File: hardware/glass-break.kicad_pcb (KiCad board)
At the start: 2 copper layers, 90 x 57 mm, 25 parts, among them P1 USB_OTG, U11 SPX3819

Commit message: layout update
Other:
- board outline removed
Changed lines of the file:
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@@
     (links 47)
     (no_connects 30)
-    (area 0 0 0 0)
+    (area 113.924999 32.924999 204.075001 129.878601)
     (thickness 1.6)
-    (drawings 6)
+    (drawings 19)
     (tracks 0)
     (zones 0)
@@
     )
   )
-  (gr_line (start 133 87) (end 133 54.5) (angle 90) (layer Edge.Cuts) (width 0.15))
-  (gr_circle (center 133 80) (end 140 80) (layer Edge.Cuts) (width 0.15))
-  (gr_line (start 114 33) (end 114 90) (angle 90) (layer Edge.Cuts) (width 0.15))
-  (gr_line (start 204 33) (end 114 33) (angle 90) (layer Edge.Cuts) (width 0.15))
-  (gr_line (start 204 90) (end 204 33) (angle 90) (layer Edge.Cuts) (width 0.15))
-  (gr_line (start 114 90) (end 204 90) (angle 90) (layer Edge.Cuts) (width 0.15))
+  (gr_line (start 172.5 85.5) (end 172.5 97.5) (angle 90) (layer Margin) (width 0.2))
+  (gr_line (start 205 85.5) (end 172.5 85.5) (angle 90) (layer Margin) (width 0.2))
+  (gr_line (start 172.5 85.5) (end 205 85.5) (angle 90) (layer Margin) (width 0.2))
+  (gr_circle (center 149.5 89) (end 149.5 85.5) (layer Margin) (width 0.2))
+  (gr_line (start 153 85.5) (end 117.5 85.5) (angle 90) (layer Margin) (width 0.2))
+  (gr_line (start 153 98.5) (end 153 85.5) (angle 90) (layer Margin) (width 0.2))
+  (gr_line (start 153 85.5) (end 153 98.5) (angle 90) (layer Margin) (width 0.2))
+  (gr_line (start 193 82.5) (end 193 94.5) (angle 90) (layer Margin) (width 0.2))
+  (gr_line (start 193 82.5) (end 205 82.5) (angle 90) (layer Margin) (width 0.2))
+  (gr_line (start 193 56.5) (end 193 44.5) (angle 90) (layer Margin) (width 0.2))
+  (gr_line (start 205 56.5) (end 193 56.5) (angle 90) (layer Margin) (width 0.2))
+  (gr_line (start 132.5 56.5) (end 132.5 44.5) (angle 90) (layer Margin) (width 0.2))
+  (gr_line (start 120.5 56.5) (end 132.5 56.5) (angle 90) (layer Margin) (width 0.2))
+  (gr_line (start 132.5 82.5) (end 120.5 82.5) (angle 90) (layer Margin) (width 0.2))
+  (gr_line (start 132.5 94.5) (end 132.5 82.5) (angle 90) (layer Margin) (width 0.2))
+  (gr_line (start 120.5 44.5) (end 120.5 94.5) (angle 90) (layer Margin) (width 0.2))
+  (gr_line (start 205 44.5) (end 120.5 44.5) (angle 90) (layer Margin) (width 0.2))
+  (gr_line (start 205 94.5) (end 205 44.5) (angle 90) (layer Margin) (width 0.2))
+  (gr_line (start 120.5 94.5) (end 205 94.5) (angle 90) (layer Margin) (width 0.2))
 )

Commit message: layout update
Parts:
- moved C1 94.1 mm to (238.5, 77.5)
- moved C2 94.1 mm to (238.5, 77.5)
- moved C3 94.1 mm to (238.5, 77.5)
- moved C4 94.1 mm to (238.5, 77.5)
- moved D1 94.1 mm to (238.5, 77.5)
- moved D2 94.1 mm to (238.5, 77.5)
- moved D3 94.1 mm to (238.5, 77.5)
- moved D4 94.1 mm to (238.5, 77.5)
- moved JP1 94.1 mm to (238.5, 77.5)
- moved JP4 94.1 mm to (238.5, 77.5)
- moved JP5 94.1 mm to (238.5, 77.5)
- moved P1 94.1 mm to (238.5, 77.5)
- moved R1 94.1 mm to (238.5, 77.5)
- moved R10 94.1 mm to (238.5, 77.5)
- moved R11 94.1 mm to (238.5, 77.5)
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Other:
- board outline added: 83.5 x 48.5 mm
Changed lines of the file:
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@@
     (area 113.924999 32.924999 204.075001 129.878601)
     (thickness 1.6)
-    (drawings 19)
+    (drawings 31)
     (tracks 0)
     (zones 0)
@@
   )
   (module Capacitors_SMD:C_0805 (layer F.Cu)
-    (at 148.5011 105.0036)
+    (at 238.5011 77.5036)
     (descr "Capacitor SMD 0805, reflow soldering, AVX (see smccp.pdf)")
     (tags "capacitor 0805")
@@
   )
   (module Capacitors_SMD:C_0805 (layer F.Cu)
-    (at 148.5011 105.0036)
+    (at 238.5011 77.5036)
     (descr "Capacitor SMD 0805, reflow soldering, AVX (see smccp.pdf)")
     (tags "capacitor 0805")
@@
   )
   (module Capacitors_SMD:C_0805 (layer F.Cu)
-    (at 148.5011 105.0036)
+    (at 238.5011 77.5036)
     (descr "Capacitor SMD 0805, reflow soldering, AVX (see smccp.pdf)")
     (tags "capacitor 0805")
@@
   )
   (module Capacitors_SMD:C_0805 (layer F.Cu)
-    (at 148.5011 105.0036)
+    (at 238.5011 77.5036)
     (descr "Capacitor SMD 0805, reflow soldering, AVX (see smccp.pdf)")
     (tags "capacitor 0805")
@@
   )
   (module LEDs:LED_0805 (layer F.Cu)
-    (at 148.5011 105.0036)
+    (at 238.5011 77.5036)
     (descr "LED 0805 smd package")
     (tags "LED 0805 SMD")
@@
   )
   (module LEDs:LED_0805 (layer F.Cu)
-    (at 148.5011 105.0036)
+    (at 238.5011 77.5036)
     (descr "LED 0805 smd package")
     (tags "LED 0805 SMD")
@@
   )
   (module LEDs:LED_0805 (layer F.Cu)
-    (at 148.5011 105.0036)
+    (at 238.5011 77.5036)
     (descr "LED 0805 smd package")
     (tags "LED 0805 SMD")
@@
   )
   (module LEDs:LED_0805 (layer F.Cu)
-    (at 148.5011 105.0036)
+    (at 238.5011 77.5036)
     (descr "LED 0805 smd package")
     (tags "LED 0805 SMD")
@@
   )
   (module Pin_Headers:Pin_Header_Angled_1x06 (layer F.Cu)
-    (at 148.5011 105.0036)
+    (at 238.5011 77.5036)
     (descr "Through hole pin header")
     (tags "pin header")
@@
   )
   (module Pin_Headers:Pin_Header_Angled_1x10 (layer F.Cu)
-    (at 148.5011 105.0036)
+    (at 238.5011 77.5036)
     (descr "Through hole pin header")
     (tags "pin header")
@@
   )
   (module Pin_Headers:Pin_Header_Angled_1x10 (layer F.Cu)
-    (at 148.5011 105.0036)
+    (at 238.5011 77.5036)
     (descr "Through hole pin header")
     (tags "pin header")
@@
   )
   (module Connect:USB_Micro-B (layer F.Cu)
-    (at 148.5011 105.0036)
+    (at 238.5011 77.5036)
     (descr "Micro USB Type B Receptacle")
     (tags "USB USB_B USB_micro USB_OTG")
@@
   )
   (module Resistors_SMD:R_0805 (layer F.Cu)
-    (at 148.5011 105.0036)
+    (at 238.5011 77.5036)
     (descr "Resistor SMD 0805, reflow soldering, Vishay (see dcrcw.pdf)")
     (tags "resistor 0805")
@@
   )
   (module Resistors_SMD:R_0805 (layer F.Cu)
-    (at 148.5011 105.0036)
+    (at 238.5011 77.5036)
     (descr "Resistor SMD 0805, reflow soldering, Vishay (see dcrcw.pdf)")
     (tags "resistor 0805")
@@
   )
   (module Resistors_SMD:R_0805 (layer F.Cu)
-    (at 148.5011 105.0036)
+    (at 238.5011 77.5036)
     (descr "Resistor SMD 0805, reflow soldering, Vishay (see dcrcw.pdf)")
     (tags "resistor 0805")
@@
   )
   (module Resistors_SMD:R_0805 (layer F.Cu)
-    (at 148.5011 105.0036)
+    (at 238.5011 77.5036)
     (descr "Resistor SMD 0805, reflow soldering, Vishay (see dcrcw.pdf)")
     (tags "resistor 0805")
@@
   )
   (module Resistors_SMD:R_0805 (layer F.Cu)
-    (at 148.5011 105.0036)
+    (at 238.5011 77.5036)
     (descr "Resistor SMD 0805, reflow soldering, Vishay (see dcrcw.pdf)")
     (tags "resistor 0805")
@@
   )
   (module Resistors_SMD:R_0805 (layer F.Cu)
-    (at 148.5011 105.0036)
+    (at 238.5011 77.5036)
     (descr "Resistor SMD 0805, reflow soldering, Vishay (see dcrcw.pdf)")
     (tags "resistor 0805")
@@
   )
   (module Resistors_SMD:R_0805 (layer F.Cu)
-    (at 148.5011 105.0036)
+    (at 238.5011 77.5036)
     (descr "Resistor SMD 0805, reflow soldering, Vishay (see dcrcw.pdf)")
     (tags "resistor 0805")
@@
   )
   (module Resistors_SMD:R_0805 (layer F.Cu)
-    (at 148.5011 105.0036)
+    (at 238.5011 77.5036)
     (descr "Resistor SMD 0805, reflow soldering, Vishay (see dcrcw.pdf)")
     (tags "resistor 0805")
@@
   )
   (module Resistors_SMD:R_0805 (layer F.Cu)
-    (at 148.5011 105.0036)
+    (at 238.5011 77.5036)
     (descr "Resistor SMD 0805, reflow soldering, Vishay (see dcrcw.pdf)")
     (tags "resistor 0805")
@@
   )
   (module Resistors_SMD:R_0805 (layer F.Cu)
-    (at 148.5011 105.0036)
+    (at 238.5011 77.5036)
     (descr "Resistor SMD 0805, reflow soldering, Vishay (see dcrcw.pdf)")
     (tags "resistor 0805")
@@
   )
   (module Resistors_SMD:R_0805 (layer F.Cu)
-    (at 148.5011 105.0036)
+    (at 238.5011 77.5036)
     (descr "Resistor SMD 0805, reflow soldering, Vishay (see dcrcw.pdf)")
     (tags "resistor 0805")
@@
   )
   (module Resistors_SMD:R_0805 (layer F.Cu)
-    (at 148.5011 105.0036)
+    (at 238.5011 77.5036)
     (descr "Resistor SMD 0805, reflow soldering, Vishay (see dcrcw.pdf)")
     (tags "resistor 0805")
@@
   )
   (module TO_SOT_Packages_SMD:SC-70-5 (layer F.Cu)
-    (at 148.5011 105.0036)
+    (at 238.5011 77.5036)
     (descr "SC70-5 SOT323-5")
     (attr smd)
@@
     )
   )
-  (gr_line (start 172.5 85.5) (end 172.5 97.5) (angle 90) (layer Margin) (width 0.2))
-  (gr_line (start 205 85.5) (end 172.5 85.5) (angle 90) (layer Margin) (width 0.2))
-  (gr_line (start 172.5 85.5) (end 205 85.5) (angle 90) (layer Margin) (width 0.2))
+  (gr_line (start 190 59) (end 191.5 59) (angle 90) (layer Edge.Cuts) (width 0.15))
+  (gr_line (start 190 45) (end 190 59) (angle 90) (layer Edge.Cuts) (width 0.15))
+  (gr_line (start 135 45) (end 190 45) (angle 90) (layer Edge.Cuts) (width 0.15))
+  (gr_line (start 121 80) (end 135 80) (angle 90) (layer Edge.Cuts) (width 0.15))
+  (gr_line (start 121 59) (end 121 80) (angle 90) (layer Edge.Cuts) (width 0.15))
+  (gr_line (start 135 59) (end 121 59) (angle 90) (layer Edge.Cuts) (width 0.15))
+  (gr_line (start 135 45) (end 135 59) (angle 90) (layer Edge.Cuts) (width 0.15))
+  (gr_line (start 204.5 59) (end 191.5 59) (angle 90) (layer Edge.Cuts) (width 0.15))
+  (gr_line (start 204.5 80) (end 204.5 59) (angle 90) (layer Edge.Cuts) (width 0.15))
+  (gr_line (start 190.5 80) (end 204.5 80) (angle 90) (layer Edge.Cuts) (width 0.15))
+  (gr_line (start 190.5 93.5) (end 190.5 80) (angle 90) (layer Edge.Cuts) (width 0.15))
+  (gr_line (start 135 93.5) (end 190.5 93.5) (angle 90) (layer Edge.Cuts) (width 0.15))
+  (gr_line (start 135 80) (end 135 93.5) (angle 90) (layer Edge.Cuts) (width 0.15))
+  (dimension 50 (width 0.3) (layer Margin)
+    (gr_text "50.000 mm" (at 214.35 69.5 270) (layer Margin)
+      (effects (font (size 1.5 1.5) (thickness 0.3)))
+    )
+    (feature1 (pts (xy 206.5 94.5) (xy 215.7 94.5)))
+    (feature2 (pts (xy 206.5 44.5) (xy 215.7 44.5)))
+    (crossbar (pts (xy 213 44.5) (xy 213 94.5)))
+    (arrow1a (pts (xy 213 94.5) (xy 212.413579 93.373496)))
+    (arrow1b (pts (xy 213 94.5) (xy 213.586421 93.373496)))
+    (arrow2a (pts (xy 213 44.5) (xy 212.413579 45.626504)))
+    (arrow2b (pts (xy 213 44.5) (xy 213.586421 45.626504)))
+  )
+  (dimension 84.5 (width 0.3) (layer Margin)
+    (gr_text "84.500 mm" (at 162.75 100.85) (layer Margin)
+      (effects (font (size 1.5 1.5) (thickness 0.3)))
+    )
+    (feature1 (pts (xy 205 96) (xy 205 102.2)))
+    (feature2 (pts (xy 120.5 96) (xy 120.5 102.2)))
+    (crossbar (pts (xy 120.5 99.5) (xy 205 99.5)))
+    (arrow1a (pts (xy 205 99.5) (xy 203.873496 100.086421)))
+    (arrow1b (pts (xy 205 99.5) (xy 203.873496 98.913579)))
+    (arrow2a (pts (xy 120.5 99.5) (xy 121.626504 100.086421)))
+    (arrow2b (pts (xy 120.5 99.5) (xy 121.626504 98.913579)))
+  )
+  (gr_circle (center 176 89) (end 172.5 89.5) (layer Margin) (width 0.2))
+  (gr_circle (center 176 50) (end 172.5 50) (layer Margin) (width 0.2))
+  (gr_circle (center 149.5 50) (end 153 49.5) (layer Margin) (width 0.2))
   (gr_circle (center 149.5 89) (end 149.5 85.5) (layer Margin) (width 0.2))
-  (gr_line (start 153 85.5) (end 117.5 85.5) (angle 90) (layer Margin) (width 0.2))
-  (gr_line (start 153 98.5) (end 153 85.5) (angle 90) (layer Margin) (width 0.2))
-  (gr_line (start 153 85.5) (end 153 98.5) (angle 90) (layer Margin) (width 0.2))
   (gr_line (start 193 82.5) (end 193 94.5) (angle 90) (layer Margin) (width 0.2))
   (gr_line (start 193 82.5) (end 205 82.5) (angle 90) (layer Margin) (width 0.2))

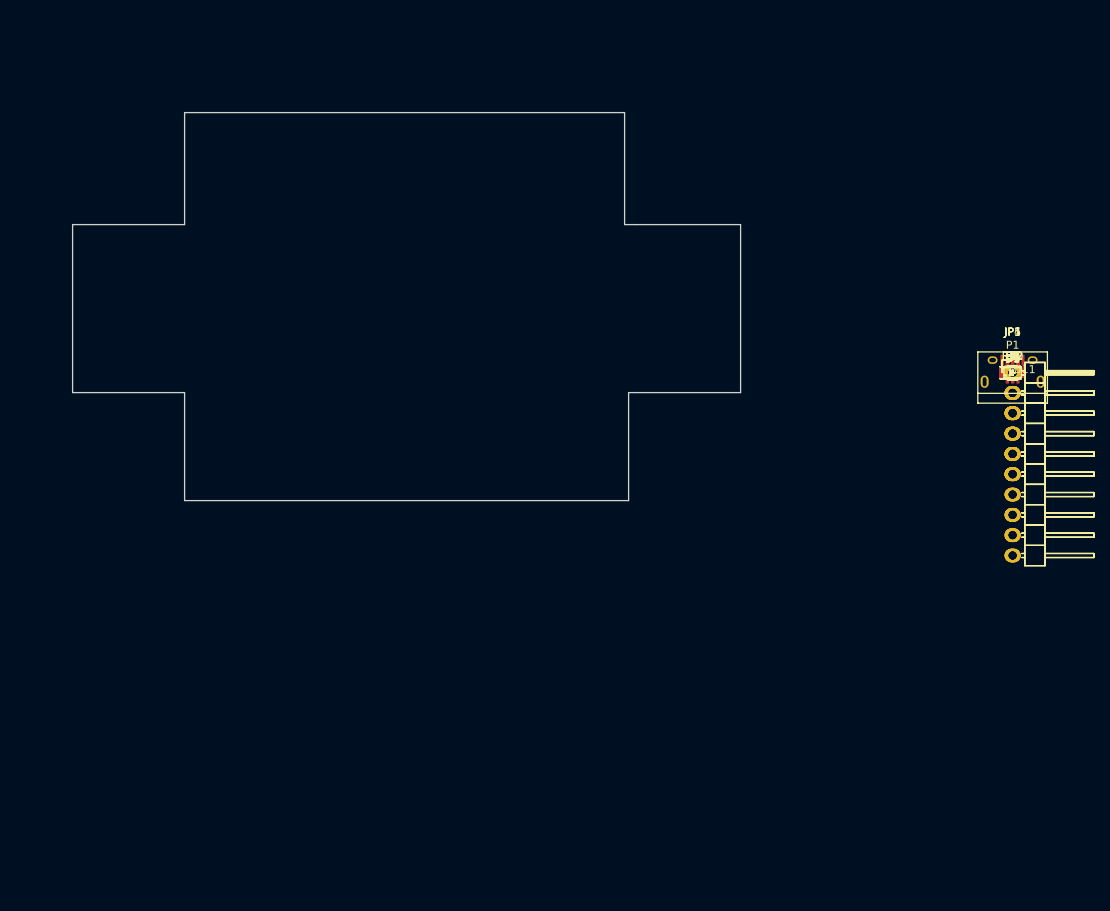
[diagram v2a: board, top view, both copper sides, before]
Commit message: added dimensions update
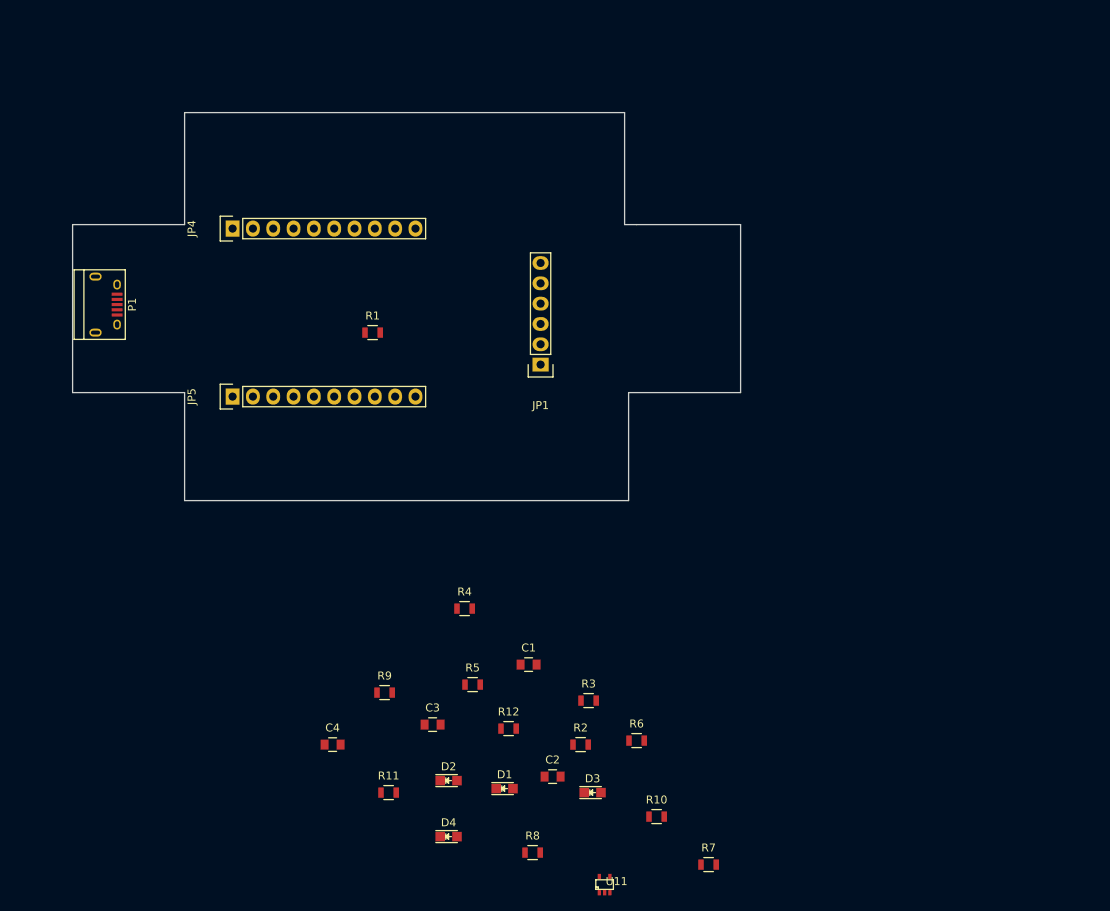
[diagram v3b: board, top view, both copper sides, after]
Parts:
- JP1: footprint Pin_Headers:Pin_Header_Angled_1x06 -> Pin_Headers:Pin_Header_Straight_1x06
- JP4, JP5: footprint Pin_Headers:Pin_Header_Angled_1x10 -> Pin_Headers:Pin_Header_Straight_1x10
- moved P1 113.8 mm to (125.0, 69.0), turned to 270 degrees
- moved JP4 99.1 mm to (141.0, 59.5), turned to 90 degrees
- moved JP5 97.5 mm to (141.0, 80.5), turned to 90 degrees
- moved C4 96.9 mm to (153.5, 124.0)
- moved R11 94.0 mm to (160.5, 130.0)
- moved D4 91.3 mm to (168.0, 135.5)
- moved R9 88.1 mm to (160.0, 117.5)
- moved D2 87.0 mm to (168.0, 128.5)
- moved R8 84.9 mm to (178.5, 137.5)
- moved C3 84.8 mm to (166.0, 121.5)
- moved D1 82.1 mm to (175.0, 129.5)
- moved U11 81.8 mm to (187.5, 141.5)
- moved R1 80.2 mm to (158.5, 72.5)
- moved R5 78.0 mm to (171.0, 116.5)
- moved R12 77.1 mm to (175.5, 122.0)
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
